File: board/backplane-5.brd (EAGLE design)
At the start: 100 x 100 mm, 142 parts, among them CN1 RJ45JACK90, U1 AMS1117-5.0, U10 RT9193, U11 KSZ9897, U12 KSZ8081MLX, U2 AMS1117-5.0, U3 AMS1117-5.0, U4 AMS1117-5.0, U5 AMS1117-5.0, U6 AMS1117-2.5, U7 AMS1117-1.2, U8 RT9193, U9 AMS1117-5.0, X1 25MHz, X2 25MHz

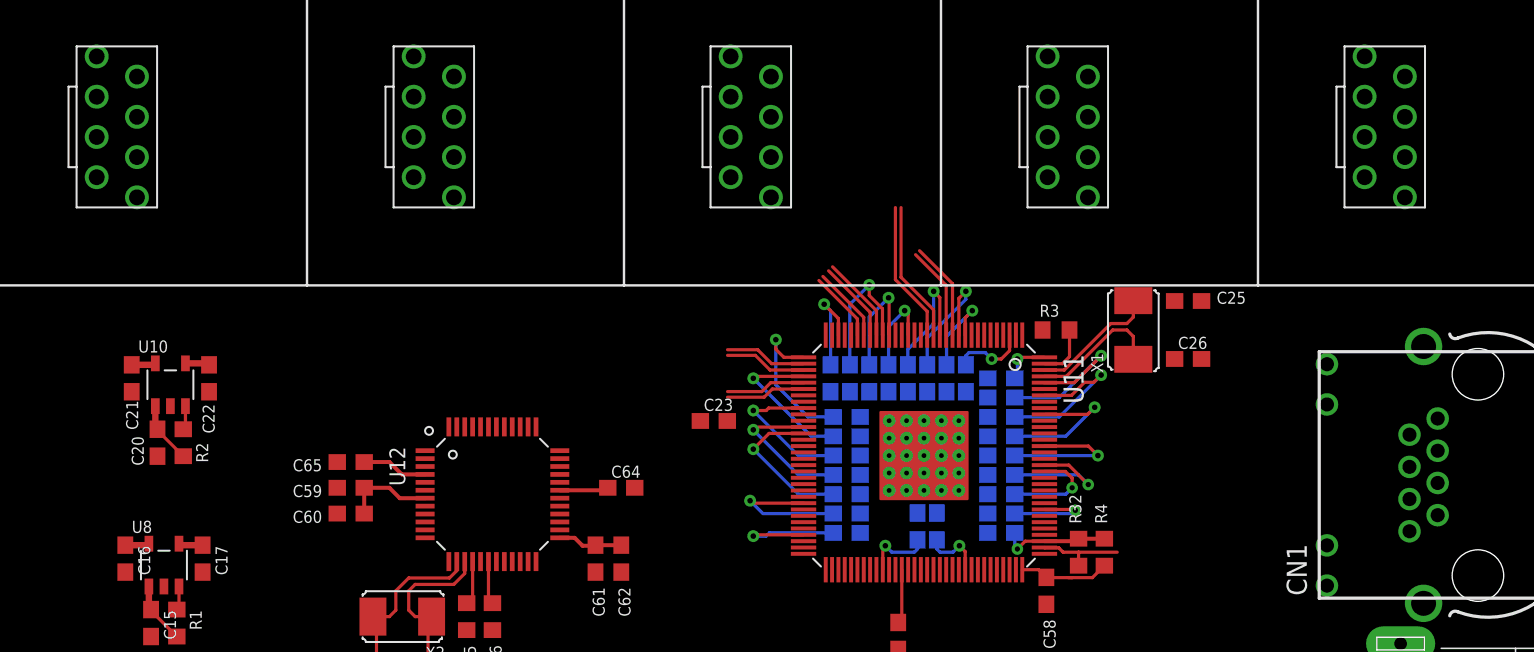
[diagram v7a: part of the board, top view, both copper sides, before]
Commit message: Routed most ethernet jacks
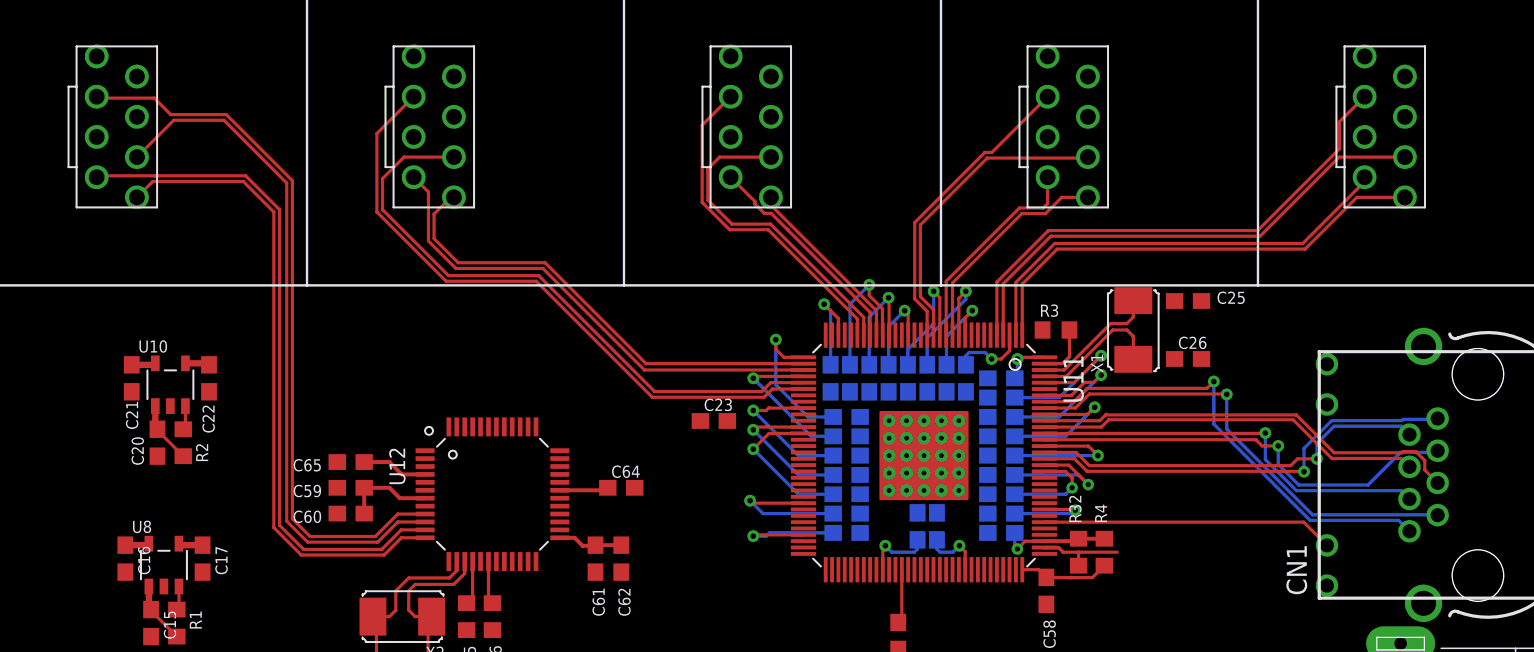
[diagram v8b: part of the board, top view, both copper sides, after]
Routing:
- net PHY6->PI5_N: track 0.00 -> 45.3 mm
- net PHY6->PI5_P: track 0.00 -> 43.2 mm
- net PI5->PHY6_N: track 0.00 -> 42.9 mm
- net PI5->PHY6_P: track 0.00 -> 40.5 mm
- net PHY4->PI4_N: track 5.01 -> 40.2 mm
- net PHY4->PI4_P: track 5.03 -> 38.6 mm
- net PHY1->PI1_N: track 0.00 -> 32.4 mm
- net PHY1->PI1_P: track 0.00 -> 31.9 mm
- net PI1->PHY1_P: track 0.00 -> 29.6 mm
- net PHY5D_P: track 0.00 -> 29.6 mm, vias 0 -> 1
- net PHY5D_N: track 0.00 -> 29.0 mm, vias 0 -> 1
- net PI1->PHY1_N: track 0.00 -> 28.2 mm
- net PHY5B_P: track 0.00 -> 27.6 mm, vias 0 -> 1
- net PHY5A_P: track 0.00 -> 27.4 mm, vias 0 -> 1
- net PHY5C_N: track 0.00 -> 27.2 mm
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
